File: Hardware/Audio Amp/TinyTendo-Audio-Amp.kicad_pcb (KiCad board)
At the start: 2 copper layers, 55 x 33.8 mm, 14 parts, among them J1 Conn_Coaxial, J2 MJ-3523-SMT, U1 LM4865M

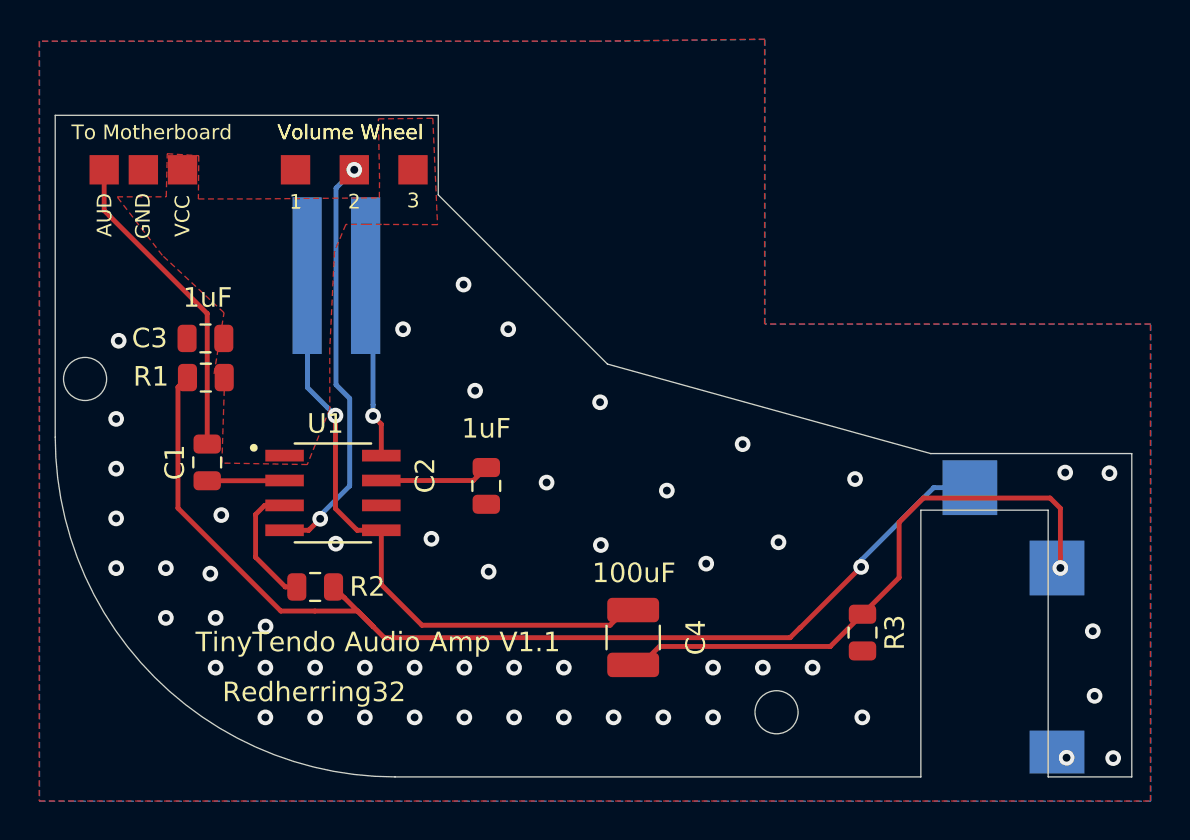
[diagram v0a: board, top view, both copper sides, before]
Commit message: + Corrected duplicate reference error in Chargeboost.sch
+ Made changes to Audio Amp PCB to improve screwpost locations

+ Made changes to Button PCB to improve screwpost locations

+ Moved screen up 6mm to even out bezels on shell

+ Altered shell to improve screwpost placement, and add optional suppport for threaded inserts

+ Added 2 new shell variants, 1 with a logo via multicolor printing and threaded inserts, 1 with just threaded inserts
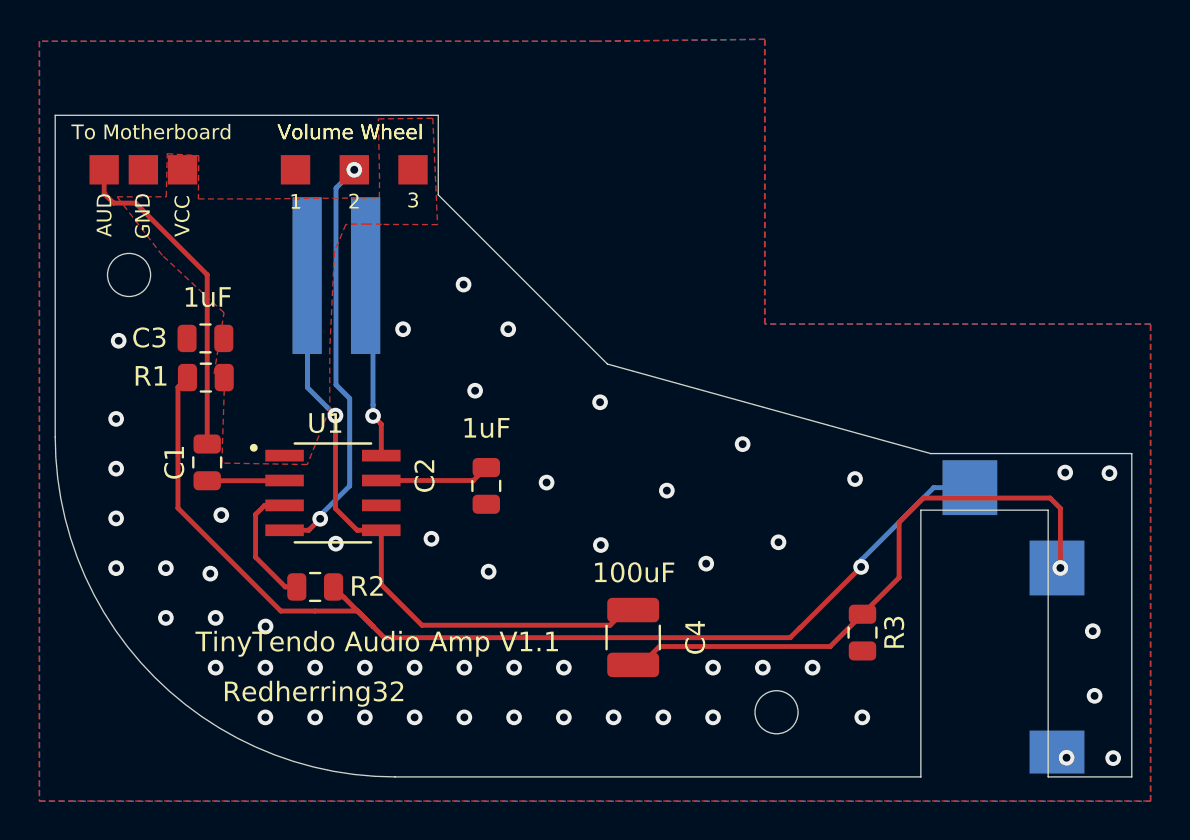
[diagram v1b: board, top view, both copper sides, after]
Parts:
- moved   5.77 mm to (3.77, -25.6)
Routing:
- net Net-(C1-Pad2): track 16.2 -> 16.9 mm
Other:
- net class Default removed
